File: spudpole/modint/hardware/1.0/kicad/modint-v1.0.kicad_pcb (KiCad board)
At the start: 2 copper layers, 87.6 x 88.9 mm, 41 parts, among them J1 SENSOR, J2 LIMIT, J3 NMEA, J4 RELAYS, K1 SANYOU_SRD_Form_C, K2 SANYOU_SRD_Form_C, Q1 2N2219, Q2 2N2219, SW1 INSTANCE/TERM, U1 4N25, U2 4N25, U3 Teensy_3.2, U4 TEC2-2411WI, U5 MCP2551-I-P

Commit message: Revised PCB design for RS enclosure
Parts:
- removed the REF** at (129.5, 161.3)
- removed the REF** at (52.1, 161.3)
- removed the REF** at (129.5, 82.5)
- removed the REF** at (52.1, 82.5)
- added F2: 1A, Fuse:Fuse_Littelfuse_395Series, F.Cu at (206.7, 94.0)
- added REF**: MountingHole_2.7mm_M2.5_Pad, MountingHole:MountingHole_2.7mm_M2.5_Pad, F.Cu at (200.0, 98.0)
- added REF**: MountingHole_2.7mm_M2.5_Pad, MountingHole:MountingHole_2.7mm_M2.5_Pad, F.Cu at (147.0, 98.0)
- added REF**: MountingHole_2.7mm_M2.5_Pad, MountingHole:MountingHole_2.7mm_M2.5_Pad, F.Cu at (200.0, 151.0)
- added REF**: MountingHole_2.7mm_M2.5_Pad, MountingHole:MountingHole_2.7mm_M2.5_Pad, F.Cu at (147.0, 151.0)
- D5: value LED -> DN
- D6: value LED -> UP
- D7: value LED -> PWR/TX; footprint LED_THT:LED_Rectangular_W3.0mm_H2.0mm -> LED_THT:LED_Rectangular_W5.0mm_H2.0mm-3Pins
- J1: footprint Connector_PinHeader_2.54mm:PinHeader_1x03_P2.54mm_Vertical -> TerminalBlock_Phoenix:TerminalBlock_Phoenix_MPT-0,5-3-2.54_1x03_P2.54mm_Horizontal
- J2: footprint Connector_PinHeader_2.54mm:PinHeader_1x04_P2.54mm_Vertical -> TerminalBlock_Phoenix:TerminalBlock_Phoenix_MPT-0,5-4-2.54_1x04_P2.54mm_Horizontal
- J3: value NMEA -> <- NMEA; footprint Connector_PinHeader_2.54mm:PinHeader_1x04_P2.54mm_Vertical -> TerminalBlock_Phoenix:TerminalBlock_Phoenix_MPT-0,5-4-2.54_1x04_P2.54mm_Horizontal
- J4: footprint Connector_PinHeader_2.54mm:PinHeader_1x06_P2.54mm_Vertical -> TerminalBlock_Phoenix:TerminalBlock_Phoenix_MPT-0,5-6-2.54_1x06_P2.54mm_Horizontal
- U4: footprint PDJR:TMR_2-2411WI -> PDJR:TEC_2-2411WI
- moved R13 118.2 mm to (205.4, 154.9), turned to 90 degrees
- moved D7 115.9 mm to (205.4, 125.7), turned to 270 degrees
- moved R11 106.3 mm to (207.9, 134.6), turned to 180 degrees
- moved SW1 105.1 mm to (164.7, 135.9), turned to 90 degrees
- moved U2 101.8 mm to (191.4, 109.2), turned to 180 degrees
- moved D2 99.8 mm to (194.0, 110.5), turned to 90 degrees
- moved R2 99.3 mm to (191.4, 113.0), turned to 180 degrees
- moved D5 98.6 mm to (204.1, 138.4), turned to 0 degrees
- moved U1 94.3 mm to (173.7, 109.2), turned to 180 degrees
- moved R12 94.3 mm to (207.9, 142.2), turned to 180 degrees
- moved C1 93.7 mm to (168.6, 97.8), turned to 0 degrees
- moved R8 92.9 mm to (182.6, 97.8)
- moved D1 92.4 mm to (176.2, 110.5), turned to 90 degrees
- moved R1 91.8 mm to (173.7, 113.0), turned to 180 degrees
- moved R4 88.4 mm to (181.3, 104.1), turned to 270 degrees
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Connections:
- D7 pad 1: Net-(D7-Pad1) -> GND
- J3 pad 1: Net-(J3-Pad1) -> Net-(F2-Pad1)
- K1 pad 1: Net-(J4-Pad6) -> Net-(J4-Pad4)
- K1 pad 10: Net-(J4-Pad4) -> Net-(J4-Pad6)
- K2 pad 1: Net-(J4-Pad3) -> Net-(J4-Pad1)
- K2 pad 10: Net-(J4-Pad1) -> Net-(J4-Pad3)
- SW1 pad 1: Net-(J3-Pad3) -> GND
- SW1 pad 10: Net-(SW1-Pad10) -> Net-(R10-Pad2)
- SW1 pad 18: Net-(R10-Pad2) -> Net-(SW1-Pad18)
- SW1 pad 9: GND -> Net-(J3-Pad3)
- U3 pad 12: Net-(D7-Pad1) -> Net-(D7-Pad3)
- U3 pad 15: Net-(SW1-Pad10) -> Net-(SW1-Pad18)
- U3 pad 16: Net-(SW1-Pad11) -> Net-(SW1-Pad17)
- U3 pad 17: Net-(SW1-Pad12) -> Net-(SW1-Pad16)
- U3 pad 18: Net-(SW1-Pad13) -> Net-(SW1-Pad15)
- U3 pad 20: Net-(SW1-Pad15) -> Net-(SW1-Pad13)
- U3 pad 21: Net-(SW1-Pad16) -> Net-(SW1-Pad12)
- U3 pad 22: Net-(SW1-Pad17) -> Net-(SW1-Pad11)
- U4 pad 2: Net-(J3-Pad1) -> Net-(F2-Pad2)
- U4 pad 7: (no net) -> GND
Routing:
- net Net-(D7-Pad3): track 0.00 -> 117.5 mm
- net Net-(R3-Pad1): track 18.3 -> 118.6 mm
- net Net-(R10-Pad2): track 86.6 -> 2.79 mm
- net Net-(D7-Pad1): track 83.4 -> 0.00 mm
- net Net-(J3-Pad3): track 139.8 -> 65.1 mm
- net Net-(R5-Pad2): track 140.1 -> 75.1 mm
- net Net-(D3-Pad1): track 177.5 -> 239.1 mm
- net Net-(R4-Pad1): track 29.5 -> 86.0 mm
- net Net-(R6-Pad2): track 123.1 -> 86.3 mm
- net Net-(J3-Pad4): track 33.9 -> 67.2 mm
- net Net-(J2-Pad3): track 20.1 -> 53.2 mm
- net Net-(D2-Pad2): track 38.0 -> 67.7 mm
- net Net-(SW1-Pad17): track 33.8 -> 5.08 mm
- net Net-(SW1-Pad16): track 30.2 -> 5.08 mm
- net Net-(J2-Pad1): track 20.1 -> 44.5 mm
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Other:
- board size 87.6 x 88.9 mm -> 75 x 75 mm
- board text added: "2020 (c) PDJR"
- board text added: "4"
- board text added: "5"
- board text added: "6"
- board text added: "7"
- board text added: "D"
- board text added: "DN"
- board text added: "UP"
- board text removed: "..."
- board text removed: "FOR ANKREO POLE ANCHORS 2020 (c) PDJR"
- board text removed: "HI"

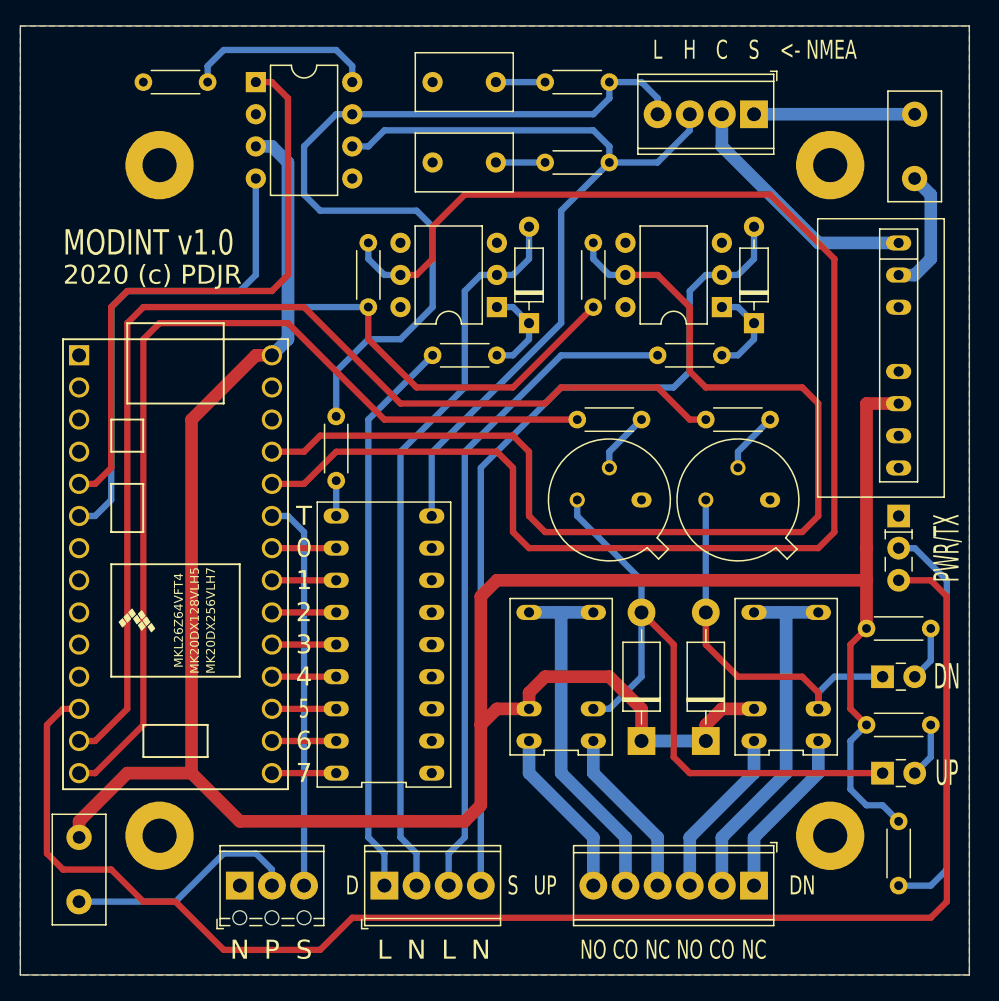
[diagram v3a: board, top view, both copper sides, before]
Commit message: Revised hardware design to include windlass motor sensor inputs
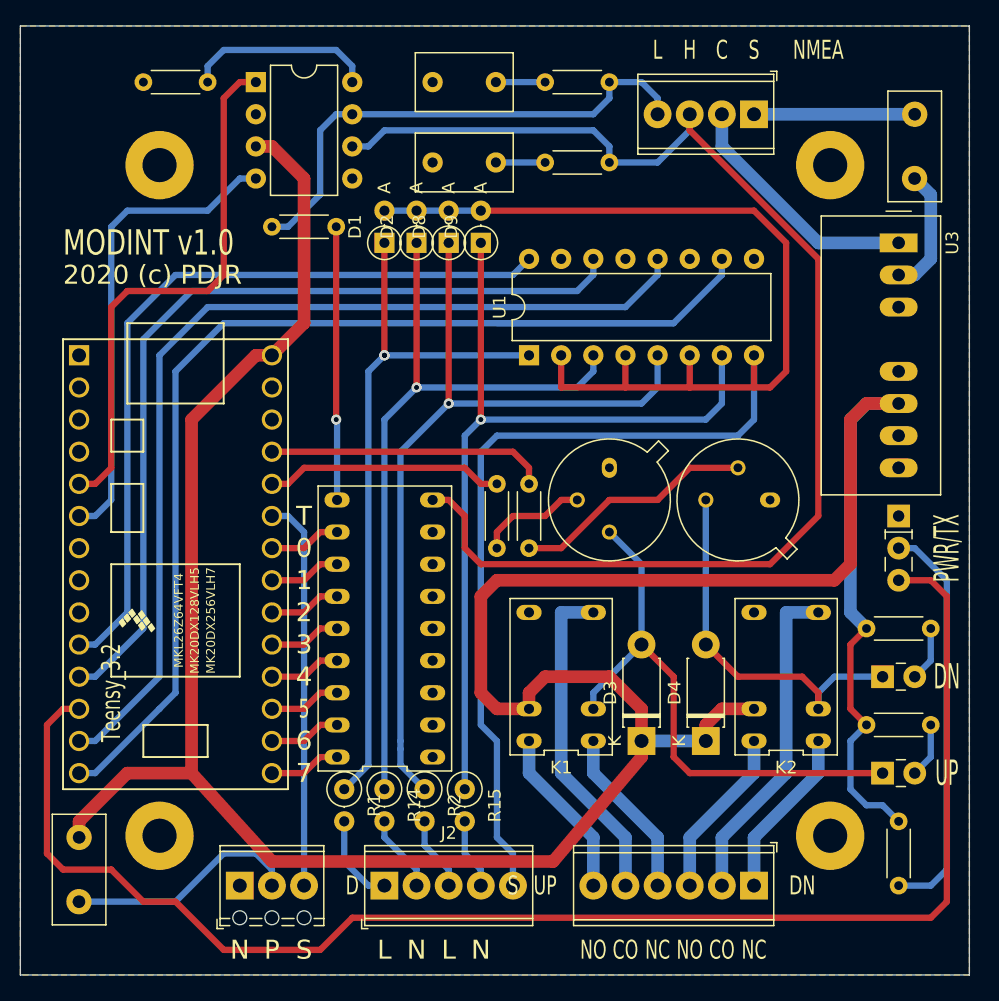
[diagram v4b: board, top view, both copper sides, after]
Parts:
- removed R3, R4: 4K7, Resistor_THT:R_Axial_DIN0204_L3.6mm_D1.6mm_P5.08mm_Horizontal
- removed U4: TEC2-2411WI, PDJR:TEC_2-2411WI
- added D8: D_Small, Diode_THT:D_DO-35_SOD27_P2.54mm_Vertical_AnodeUp, F.Cu at (169.8, 104.1)
- added D9: D_Small, Diode_THT:D_DO-35_SOD27_P2.54mm_Vertical_AnodeUp, F.Cu at (172.4, 104.1)
- added R14: 3K3, Resistor_THT:R_Axial_DIN0207_L6.3mm_D2.5mm_P2.54mm_Vertical, F.Cu at (164.8, 147.3)
- added R15: 3K3, Resistor_THT:R_Axial_DIN0207_L6.3mm_D2.5mm_P2.54mm_Vertical, F.Cu at (171.1, 147.3)
- D1, D2: value 1N4148 -> D_Small; footprint Diode_THT:D_DO-35_SOD27_P7.62mm_Horizontal -> Diode_THT:D_DO-35_SOD27_P2.54mm_Vertical_AnodeUp
- D3, D4: footprint Diode_THT:D_DO-41_SOD81_P10.16mm_Horizontal -> Diode_THT:D_DO-41_SOD81_P7.62mm_Horizontal
- J2: value LIMIT -> Screw_Terminal_01x05; footprint TerminalBlock_Phoenix:TerminalBlock_Phoenix_MPT-0,5-4-2.54_1x04_P2.54mm_Horizontal -> TerminalBlock_Phoenix:TerminalBlock_Phoenix_MPT-0,5-5-2.54_1x05_P2.54mm_Horizontal
- J3: value <- NMEA -> NMEA
- K1, K2: value SANYOU_SRD_Form_C -> RS-RELAY
- R1, R2: footprint Resistor_THT:R_Axial_DIN0204_L3.6mm_D1.6mm_P5.08mm_Horizontal -> Resistor_THT:R_Axial_DIN0207_L6.3mm_D2.5mm_P2.54mm_Vertical
- U1: value 4N25 -> CNY74-4H; footprint Package_DIP:DIP-6_W7.62mm -> Package_DIP:DIP-16_W7.62mm
- U2: value 4N25 -> Teensy_3.2; footprint Package_DIP:DIP-6_W7.62mm -> PDJR:Teensy30_31_32_LC
- U3: value Teensy_3.2 -> TEC2-2411WI; footprint PDJR:Teensy30_31_32_LC -> Converter_DCDC:Converter_DCDC_TRACO_TMR-xxxx_THT
- moved U3 62.5 mm to (205.4, 104.1)
- moved U2 47.7 mm to (148.3, 129.5), turned to 270 degrees
- moved R2 41.6 mm to (167.9, 147.3), turned to 270 degrees
- moved R1 36.4 mm to (161.6, 147.3), turned to 270 degrees
- moved D2 27.4 mm to (167.3, 104.1)
- moved R6 21.6 mm to (176.2, 128.3), turned to 90 degrees
- moved R10 15.8 mm to (155.9, 102.9), turned to 0 degrees
- moved R5 15.3 mm to (173.7, 128.3), turned to 90 degrees
- moved D1 13.1 mm to (164.8, 104.1)
- moved U1 4.58 mm to (176.2, 113.0), turned to 90 degrees
- moved Q1 3.59 mm to (182.6, 121.9), turned to 270 degrees
- moved SW1 1.27 mm to (164.8, 134.6)
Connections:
- D2 pad 2: Net-(D2-Pad2) -> Net-(D1-Pad2)
- J2 pad 2: Net-(D1-Pad2) -> Net-(J2-Pad2)
- J2 pad 4: Net-(D2-Pad2) -> Net-(J2-Pad4)
- K1 pad 6: Net-(J4-Pad5) -> (no net)
- K2 pad 6: Net-(J4-Pad2) -> (no net)
- R2 pad 1: Net-(D2-Pad1) -> Net-(D8-Pad1)
- U1 pad 3: (no net) -> Net-(D2-Pad1)
- U1 pad 4: GND -> Net-(D1-Pad2)
- U1 pad 5: Net-(R3-Pad1) -> Net-(D8-Pad1)
- U1 pad 6: (no net) -> Net-(D1-Pad2)
- U2 pad 1: Net-(D2-Pad1) -> GND
- U2 pad 2: Net-(D2-Pad2) -> (no net)
- U2 pad 4: GND -> (no net)
- U2 pad 5: Net-(R4-Pad1) -> Net-(U2-Pad5)
- U2 pad 6: (no net) -> Net-(U2-Pad6)
- U3 pad 1: GND -> Net-(J3-Pad2)
- U3 pad 2: (no net) -> Net-(F2-Pad2)
- U3 pad 5: Net-(U3-Pad5) -> (no net)
- U3 pad 6: Net-(U3-Pad6) -> Net-(D3-Pad1)
- U3 pad 7: (no net) -> GND
- U5 pad 1: Net-(U3-Pad5) -> Net-(U2-Pad5)
- U5 pad 4: Net-(U3-Pad6) -> Net-(U2-Pad6)
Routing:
- net Net-(R3-Pad1): track 118.6 -> 0.00 mm
- net Net-(U1-Pad10): track 0.00 -> 97.2 mm
- net Net-(R4-Pad1): track 86.0 -> 0.00 mm
- net Net-(U1-Pad12): track 0.00 -> 77.1 mm
- net Net-(D1-Pad2): track 58.3 -> 134.5 mm
- net Net-(U1-Pad14): track 0.00 -> 68.5 mm
- net Net-(D2-Pad2): track 67.7 -> 0.00 mm
- net Net-(D9-Pad1): track 0.00 -> 67.1 mm, vias 0 -> 1
- net Net-(D8-Pad1): track 0.00 -> 65.1 mm, vias 0 -> 1
- net Net-(R6-Pad2): track 86.3 -> 22.1 mm
- net Net-(U1-Pad16): track 0.00 -> 61.6 mm
- net Net-(R5-Pad2): track 75.1 -> 18.8 mm
- net Net-(D2-Pad1): track 7.40 -> 60.0 mm, vias 0 -> 1
- net Net-(D1-Pad1): track 7.40 -> 55.9 mm, vias 0 -> 2
- net Net-(U3-Pad5): track 47.8 -> 0.00 mm
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
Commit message: SHaking down
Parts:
- moved SW1 1.91 mm to (164.8, 132.7)
- moved R1 1.27 mm to (161.6, 146.1)
- moved R14 1.27 mm to (164.8, 146.1)
- moved R15 1.27 mm to (171.1, 146.1)
- moved R2 1.27 mm to (167.9, 146.1)
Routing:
- net Net-(R6-Pad2): track 22.1 -> 24.3 mm, vias 0 -> 1
- net Net-(J3-Pad3): track 102.9 -> 104.8 mm
- net Net-(R10-Pad2): track 21.6 -> 19.7 mm, vias 1 -> 0
- net Net-(J2-Pad4): track 5.61 -> 6.88 mm
- net Net-(J2-Pad3): track 5.87 -> 7.14 mm
- net Net-(J2-Pad2): track 6.13 -> 7.40 mm
- net Net-(J2-Pad1): track 7.14 -> 8.41 mm
- net Net-(D9-Pad1): track 67.1 -> 65.8 mm
- net Net-(D8-Pad1): track 65.1 -> 63.9 mm
- net Net-(D2-Pad1): track 60.0 -> 58.7 mm
- net Net-(D1-Pad1): track 55.9 -> 54.7 mm, vias 2 -> 1
- net Net-(R5-Pad2): track 18.8 -> 19.9 mm, vias 0 -> 1
- net Net-(SW1-Pad18): track 5.68 -> 6.68 mm
- net Net-(SW1-Pad16): track 5.68 -> 6.68 mm
- net Net-(SW1-Pad15): track 5.68 -> 6.68 mm
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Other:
- board text added: "+5"
- board text added: "DK"
- board text added: "MODINT 1.0"
- board text added: "SIG"
- board text added: "ST"
- board text removed: "D"
- board text removed: "MODINT v1.0"
- board text removed: "P"

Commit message: Many tweaks
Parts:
- moved J4 12.7 mm to (181.3, 154.9), turned to 0 degrees
- moved D1 1.42 mm to (163.5, 104.8)
- moved D4 0.90 mm to (173.0, 104.8)
- moved D2 0.90 mm to (166.7, 104.8)
- moved R13 0.90 mm to (155.2, 102.2)
- moved D3 0.64 mm to (169.8, 104.8)
- renumbered D8 to D3, D9 to D4, D7 to D5, D5 to D6, D6 to D7, D3 to D8, D4 to D9, R12 to R10, R8 to R11, R9 to R12, R10 to R13, R14 to R2, R2 to R3, R15 to R4, R13 to R7, R7 to R8, R11 to R9, U5 to U4
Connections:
- K1 pad 1: Net-(J4-Pad4) -> Net-(J4-Pad3)
- K1 pad 10: Net-(J4-Pad6) -> Net-(J4-Pad1)
- K1 pad 5: Net-(J4-Pad5) -> Net-(J4-Pad2)
- K2 pad 1: Net-(J4-Pad1) -> Net-(J4-Pad6)
- K2 pad 10: Net-(J4-Pad3) -> Net-(J4-Pad4)
- K2 pad 5: Net-(J4-Pad2) -> Net-(J4-Pad5)
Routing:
- net Net-(D4-Pad1): track 65.8 -> 64.8 mm
- net Net-(R13-Pad2): track 19.7 -> 20.6 mm
- net Net-(D1-Pad2): track 134.5 -> 133.6 mm
- net Net-(D8-Pad1): track 234.3 -> 233.8 mm
